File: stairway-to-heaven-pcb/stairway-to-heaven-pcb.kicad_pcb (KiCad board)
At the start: 2 copper layers, 99.8 x 97.3 mm, 67 parts, among them J1 Conn_01x04_Male, J10 Conn_01x04_Male, J11 Conn_01x04_Male, J12 Conn_01x04_Male, J13 Conn_01x04_Male, J14 Conn_01x04_Male, J15 PJ-063AH, J2 Conn_01x04_Male, J3 Conn_01x04_Male, J4 Conn_01x04_Male, J5 Conn_01x04_Male, J6 Conn_01x04_Male, J7 Conn_01x04_Male, J8 Conn_01x04_Male, J9 Conn_01x04_Male, Q1 FDN337N, Q10 FDN337N, Q11 FDN337N, Q12 FDN337N, Q13 FDN337N, Q14 FDN337N, Q15 FDN337N, Q16 FDN337N, Q17 FDN337N, Q18 FDN337N, Q19 FDN337N, Q2 FDN337N, Q20 FDN337N, Q21 FDN337N, Q22 FDN337N, Q23 FDN337N, Q24 FDN337N, Q25 FDN337N, Q26 FDN337N, Q27 FDN337N, Q28 FDN337N, Q29 FDN337N, Q3 FDN337N, Q30 FDN337N, Q31 FDN337N, Q32 FDN337N, Q33 FDN337N, Q34 FDN337N, Q35 FDN337N, Q36 FDN337N, Q37 FDN337N, Q38 FDN337N, Q39 FDN337N, Q4 FDN337N, Q40 FDN337N, Q41 FDN337N, Q42 FDN337N, Q5 FDN337N, Q6 FDN337N, Q7 FDN337N, Q8 FDN337N, Q9 FDN337N, U1 MEGA_PRO_EMBED_CH340G_{slash}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, U2 LM2575T-5.0

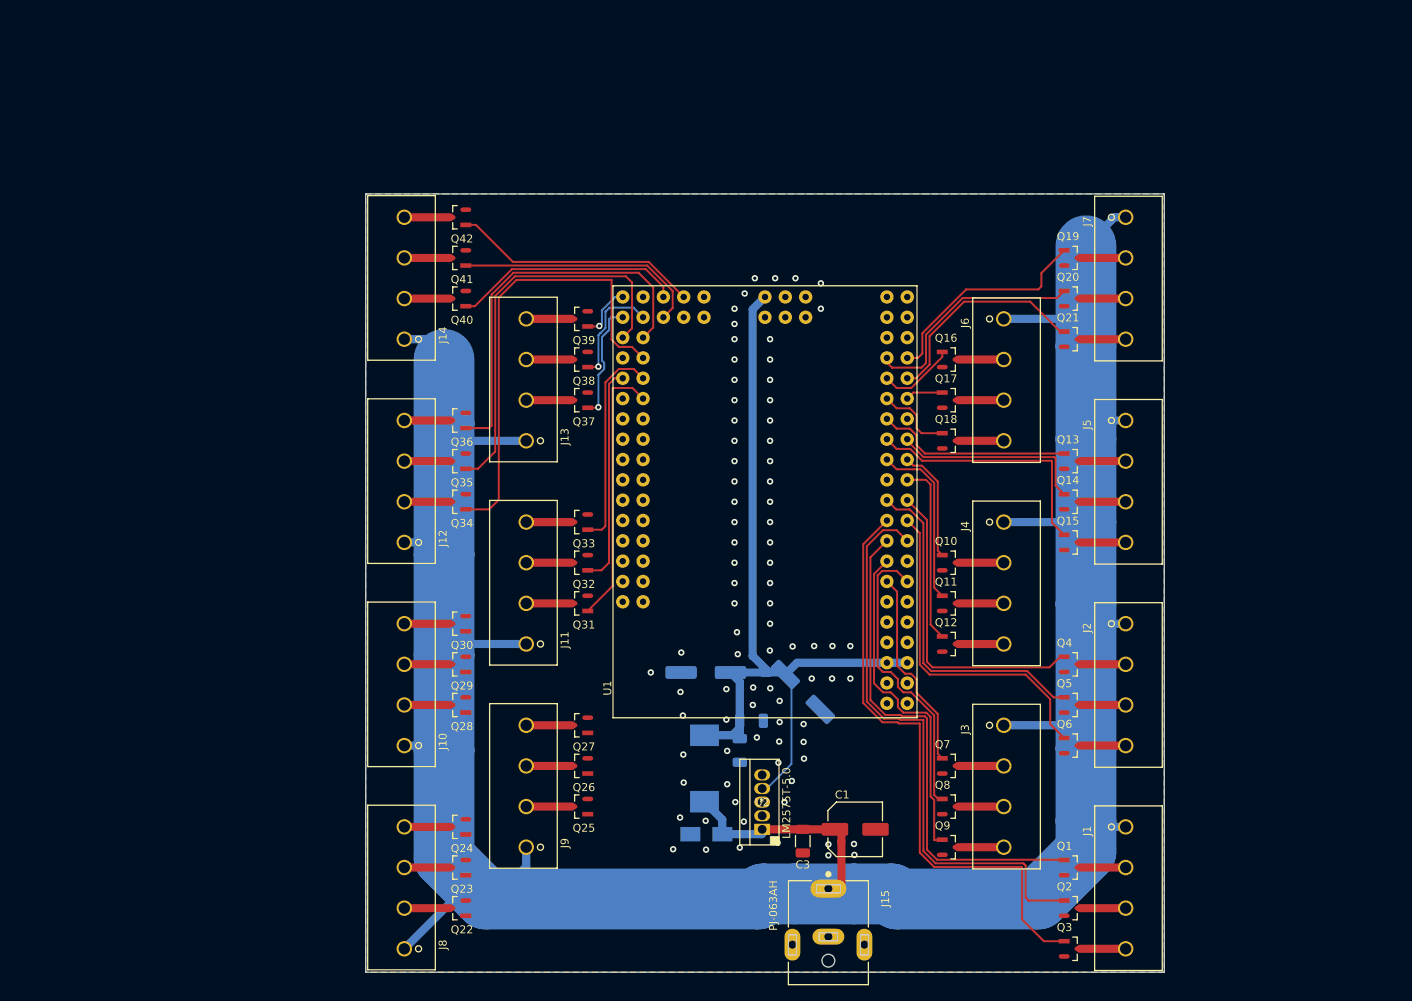
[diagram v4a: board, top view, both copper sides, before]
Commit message: replace 5V side, via galore, lots of ground areas checked, rest of the signals places
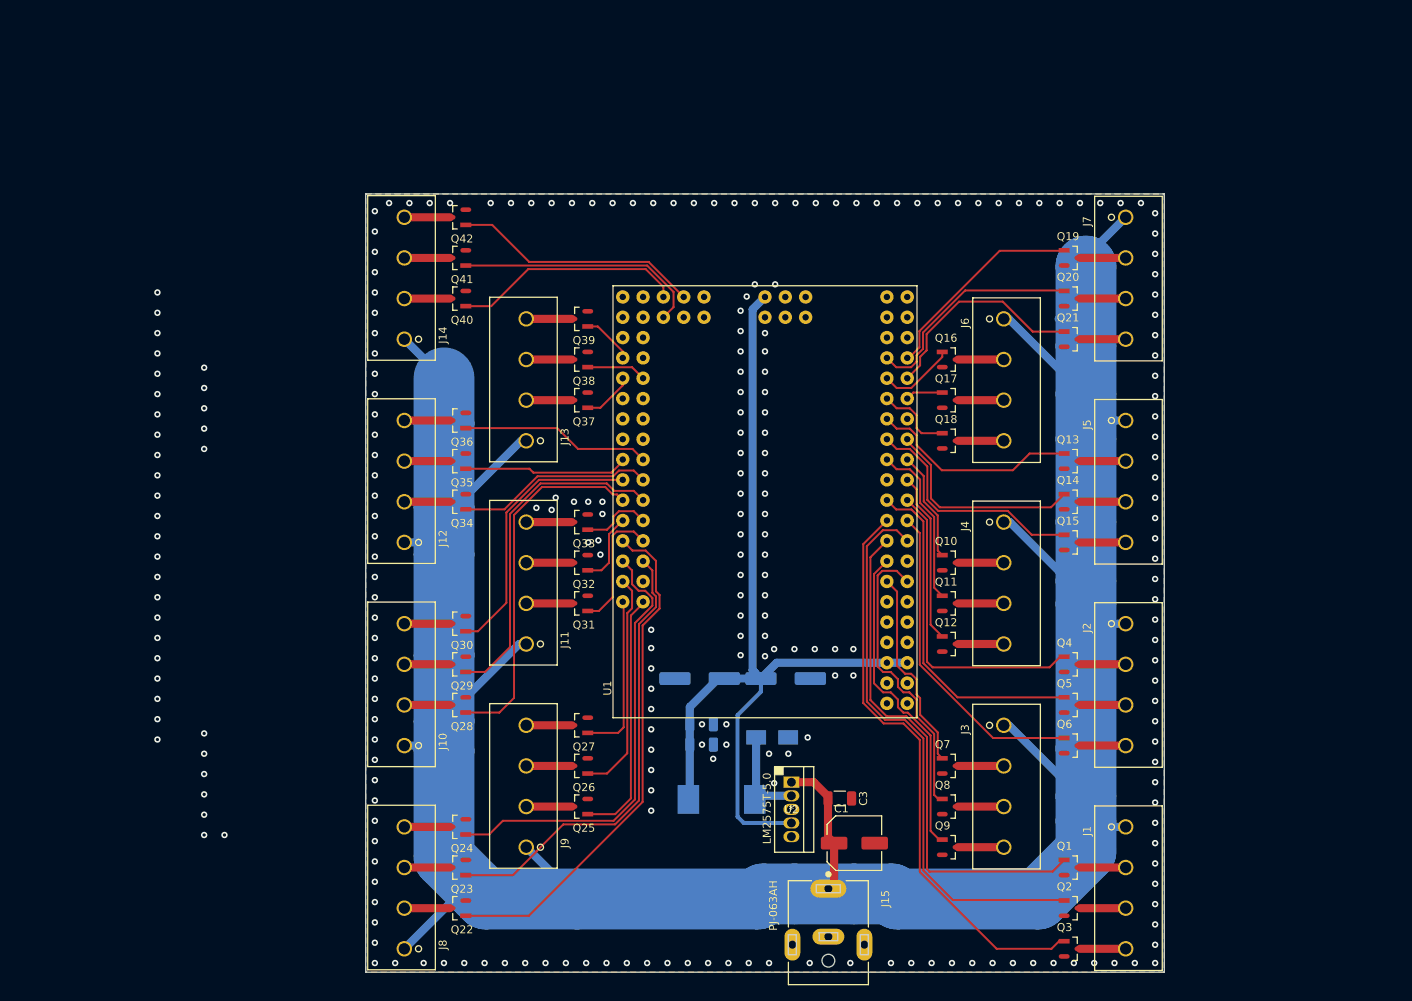
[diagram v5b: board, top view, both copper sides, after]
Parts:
- moved D1 14.6 mm to (152.0, 109.5), turned to 0 degrees
- moved C3 7.06 mm to (160.5, 117.1), turned to 180 degrees
- moved C6 6.26 mm to (143.2, 107.8)
- moved C5 4.83 mm to (143.2, 110.4), turned to 0 degrees
- moved L1 4.43 mm to (145.7, 117.2), turned to 180 degrees
- moved U2 3.77 mm to (154.4, 118.5), turned to 0 degrees
- moved C4 2.72 mm to (153.7, 102.1), turned to 0 degrees
- moved C1 1.73 mm to (162.3, 122.7)
- moved C2 1.08 mm to (143.0, 102.1)
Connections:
- Q25 pad 1: /Fets9/G_EN -> /LED9G_EN
- Q26 pad 1: /LED9R_EN -> /Fets9/R_EN
- U1 pad A0: unconnected-(U1-PadA0) -> /Fets9/B_EN
- U1 pad A1: unconnected-(U1-PadA1) -> /LED9G_EN
- U1 pad A10: unconnected-(U1-PadA10) -> /Fets10/G_EN
- U1 pad A11: unconnected-(U1-PadA11) -> /LED10R_EN
- U1 pad A12: unconnected-(U1-PadA12) -> /Fets10/B_EN
- U1 pad A13: unconnected-(U1-PadA13) -> /Fets12/G_EN
- U1 pad A14: unconnected-(U1-PadA14) -> /LED12R_EN
- U1 pad A15: unconnected-(U1-PadA15) -> /Fets12/B_EN
- U1 pad A2: unconnected-(U1-PadA2) -> /Fets9/R_EN
- U1 pad A4: unconnected-(U1-PadA4) -> /Fets8/B_EN
- U1 pad A5: unconnected-(U1-PadA5) -> /LED8R_EN
- U1 pad A6: unconnected-(U1-PadA6) -> /Fets8/G_EN
- U1 pad A7: unconnected-(U1-PadA7) -> /Fets11/G_EN
- U1 pad A8: unconnected-(U1-PadA8) -> /LED11R_EN
- U1 pad A9: unconnected-(U1-PadA9) -> /Fets11/B_EN
- U1 pad D27: /Fets8/B_EN -> unconnected-(U1-PadD27)
- U1 pad D28: /LED8R_EN -> unconnected-(U1-PadD28)
- U1 pad D29: /Fets8/G_EN -> unconnected-(U1-PadD29)
- U1 pad D30: /Fets9/B_EN -> unconnected-(U1-PadD30)
- U1 pad D31: /LED9R_EN -> unconnected-(U1-PadD31)
- U1 pad D32: /Fets9/G_EN -> unconnected-(U1-PadD32)
- U1 pad D34: /Fets10/B_EN -> unconnected-(U1-PadD34)
- U1 pad D35: /LED10R_EN -> unconnected-(U1-PadD35)
- U1 pad D36: /Fets10/G_EN -> unconnected-(U1-PadD36)
- U1 pad D37: /Fets11/G_EN -> unconnected-(U1-PadD37)
- U1 pad D38: /LED11R_EN -> /Fets13/G_EN
- U1 pad D39: /Fets11/B_EN -> /LED13R_EN
- U1 pad D40: unconnected-(U1-PadD40) -> /Fets13/B_EN
- U1 pad D41: /Fets12/G_EN -> unconnected-(U1-PadD41)
- U1 pad D42: /LED12R_EN -> unconnected-(U1-PadD42)
- U1 pad D43: /Fets12/B_EN -> unconnected-(U1-PadD43)
- U1 pad D44: /Fets13/G_EN -> unconnected-(U1-PadD44)
- U1 pad D45: /LED13R_EN -> unconnected-(U1-PadD45)
- U1 pad D46: /Fets13/B_EN -> unconnected-(U1-PadD46)
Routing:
- net /Fets8/G_EN: track 0.00 -> 64.4 mm
- net /LED8R_EN: track 0.00 -> 57.0 mm
- net /Fets8/B_EN: track 0.00 -> 55.7 mm
- net /Fets10/G_EN: track 0.00 -> 45.4 mm
- net /LED10R_EN: track 0.00 -> 42.5 mm
- net /Fets10/B_EN: track 0.00 -> 34.1 mm
- net /Fets12/G_EN: track 57.3 -> 24.7 mm
- net /LED9G_EN: track 0.00 -> 31.4 mm
- net /LED12R_EN: track 49.8 -> 20.6 mm
- net /Fets9/R_EN: track 0.00 -> 28.8 mm
- net +12V: track 356.4 -> 383.8 mm
- net /Fets12/B_EN: track 48.6 -> 23.8 mm
- net /Fets9/B_EN: track 0.00 -> 20.5 mm
- net /LED11R_EN: track 27.4 -> 9.05 mm
- net /Fets11/G_EN: track 33.5 -> 16.0 mm
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
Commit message: Vias galore
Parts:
- added R1: 0R, Resistor_SMD:R_1206_3216Metric, F.Cu at (169.5, 130.2)
- added R2: 0R, Resistor_SMD:R_1206_3216Metric, F.Cu at (130.3, 129.5)
- added R3: 0R, Resistor_SMD:R_1206_3216Metric, F.Cu at (169.5, 126.4)
- moved C1 0.89 mm to (162.3, 121.8)
- moved C3 0.63 mm to (160.5, 116.5)
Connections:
- U1 pad D23: /Fets7/B_EN -> unconnected-(U1-PadD23)
- U1 pad D24: /LED7R_EN -> unconnected-(U1-PadD24)
- U1 pad D25: /Fets7/G_EN -> unconnected-(U1-PadD25)
- U1 pad D29: unconnected-(U1-PadD29) -> /Fets7/B_EN
- U1 pad D30: unconnected-(U1-PadD30) -> /LED7R_EN
- U1 pad D31: unconnected-(U1-PadD31) -> /Fets7/G_EN
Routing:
- net /Fets7/B_EN: track 27.0 -> 20.4 mm
- net /LED1R_EN: track 70.5 -> 76.3 mm
- net /Fets1/B_EN: track 72.0 -> 77.0 mm
- net +12V: track 383.8 -> 378.9 mm
- net /LED7R_EN: track 28.3 -> 23.6 mm
- net /Fets7/G_EN: track 26.4 -> 22.0 mm
- net /Fets8/G_EN: track 64.4 -> 68.2 mm
- net /LED8R_EN: track 57.0 -> 60.8 mm
- net /Fets1/G_EN: track 64.1 -> 67.9 mm
- net /Fets5/B_EN: track 29.6 -> 32.1 mm
- net /Fets6/G_EN: track 9.66 -> 8.28 mm
- net /Fets3/G_EN: track 39.2 -> 40.0 mm
- net /Fets2/G_EN: track 25.4 -> 26.0 mm
- net GND: vias 256 -> 691

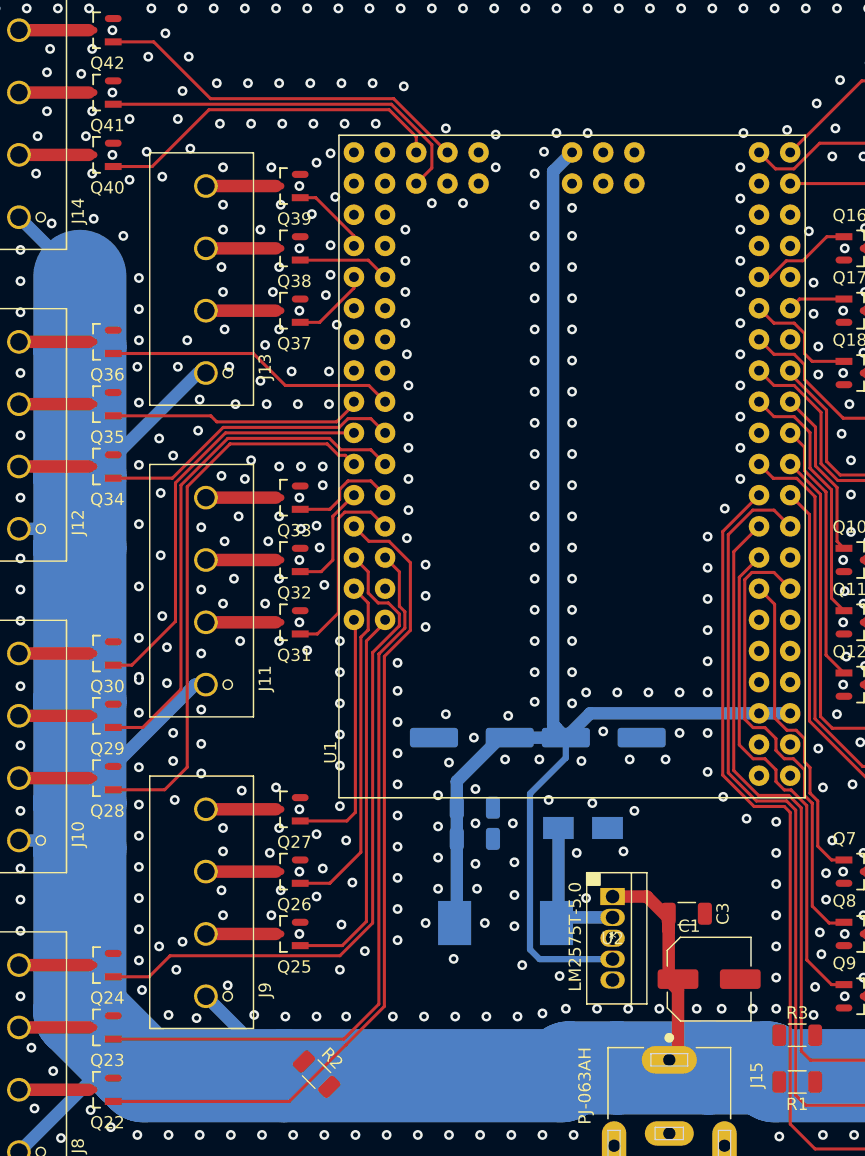
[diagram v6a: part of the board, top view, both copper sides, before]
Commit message: Pull-up resistors. Some sw work.
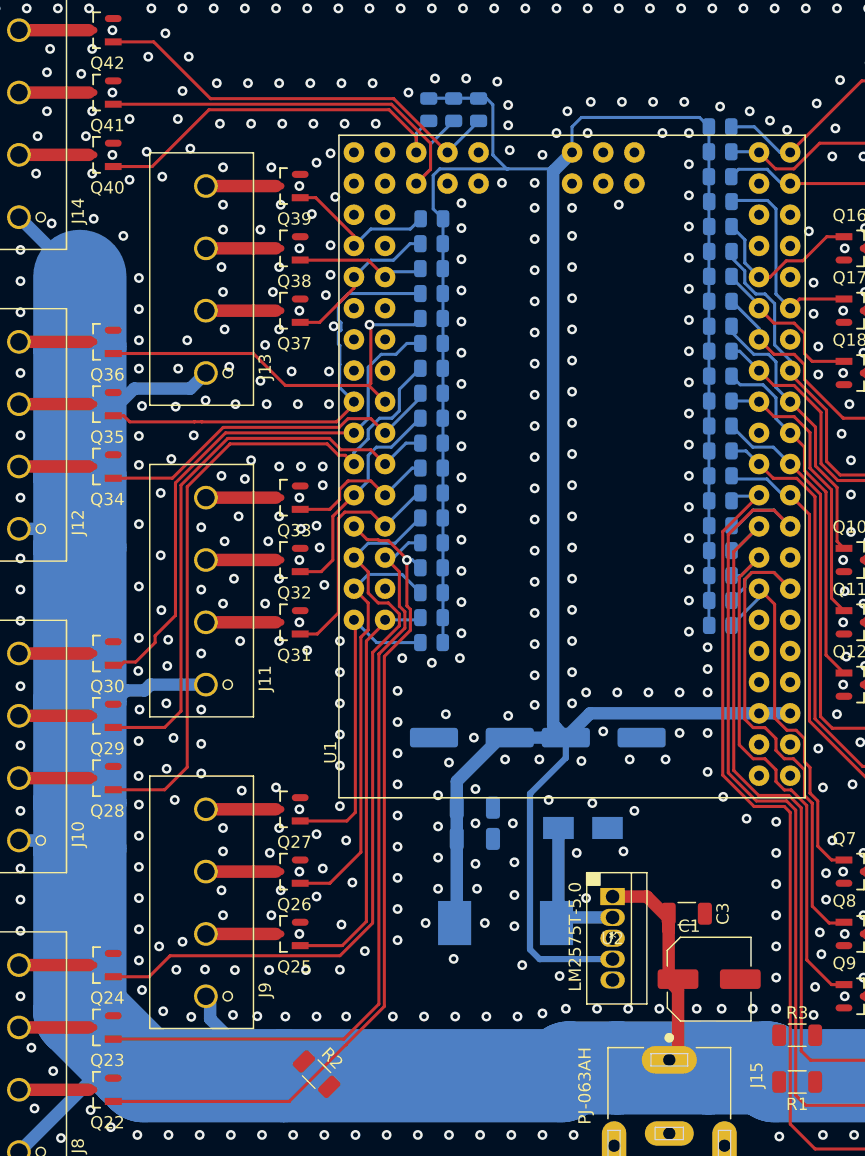
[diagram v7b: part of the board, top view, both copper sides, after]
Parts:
- added R10: 50k, Resistor_SMD:R_0805_2012Metric, B.Cu at (163.2, 93.0)
- added R11: 50k, Resistor_SMD:R_0805_2012Metric, B.Cu at (163.2, 90.9)
- added R12: 50k, Resistor_SMD:R_0805_2012Metric, B.Cu at (163.2, 88.9)
- added R13: 50k, Resistor_SMD:R_0805_2012Metric, B.Cu at (163.2, 68.6)
- added R14: 50k, Resistor_SMD:R_0805_2012Metric, B.Cu at (163.2, 74.7)
- added R15: 50k, Resistor_SMD:R_0805_2012Metric, B.Cu at (163.2, 72.6)
- added R16: 50k, Resistor_SMD:R_0805_2012Metric, B.Cu at (163.2, 66.5)
- added R17: 50k, Resistor_SMD:R_0805_2012Metric, B.Cu at (163.2, 62.5)
- added R18: 50k, Resistor_SMD:R_0805_2012Metric, B.Cu at (163.2, 70.6)
- added R19: 50k, Resistor_SMD:R_0805_2012Metric, B.Cu at (163.2, 60.5)
- added R20: 50k, Resistor_SMD:R_0805_2012Metric, B.Cu at (163.2, 58.4)
- added R21: 50k, Resistor_SMD:R_0805_2012Metric, B.Cu at (163.2, 64.5)
- added R22: 50k, Resistor_SMD:R_0805_2012Metric, B.Cu at (163.2, 52.3)
- added R23: 50k, Resistor_SMD:R_0805_2012Metric, B.Cu at (163.2, 54.4)
- added R24: 50k, Resistor_SMD:R_0805_2012Metric, B.Cu at (163.2, 56.4)
- added R25: 50k, Resistor_SMD:R_0805_2012Metric, B.Cu at (139.7, 88.3)
- added R26: 50k, Resistor_SMD:R_0805_2012Metric, B.Cu at (139.7, 86.2)
- added R27: 50k, Resistor_SMD:R_0805_2012Metric, B.Cu at (139.7, 84.2)
- added R28: 50k, Resistor_SMD:R_0805_2012Metric, B.Cu at (139.7, 92.3)
- added R29: 50k, Resistor_SMD:R_0805_2012Metric, B.Cu at (139.7, 90.3)
- added R30: 50k, Resistor_SMD:R_0805_2012Metric, B.Cu at (139.7, 94.4)
- added R31: 50k, Resistor_SMD:R_0805_2012Metric, B.Cu at (139.7, 72.0)
- added R32: 50k, Resistor_SMD:R_0805_2012Metric, B.Cu at (139.7, 78.1)
- added R33: 50k, Resistor_SMD:R_0805_2012Metric, B.Cu at (139.7, 70.0)
- added R34: 50k, Resistor_SMD:R_0805_2012Metric, B.Cu at (139.7, 82.2)
- added R35: 50k, Resistor_SMD:R_0805_2012Metric, B.Cu at (139.7, 76.1)
- added R36: 50k, Resistor_SMD:R_0805_2012Metric, B.Cu at (139.7, 80.1)
- added R37: 50k, Resistor_SMD:R_0805_2012Metric, B.Cu at (139.7, 74.0)
- added R38: 50k, Resistor_SMD:R_0805_2012Metric, B.Cu at (139.7, 65.9)
- added R39: 50k, Resistor_SMD:R_0805_2012Metric, B.Cu at (139.7, 67.9)
- added R4: 50k, Resistor_SMD:R_0805_2012Metric, B.Cu at (163.2, 86.9)
- added R40: 50k, Resistor_SMD:R_0805_2012Metric, B.Cu at (139.7, 61.8)
- added R41: 50k, Resistor_SMD:R_0805_2012Metric, B.Cu at (139.7, 63.9)
- added R42: 50k, Resistor_SMD:R_0805_2012Metric, B.Cu at (139.7, 59.8)
- added R43: 50k, Resistor_SMD:R_0805_2012Metric, B.Cu at (139.4, 50.9)
- added R44: 50k, Resistor_SMD:R_0805_2012Metric, B.Cu at (141.5, 50.9)
- added R45: 50k, Resistor_SMD:R_0805_2012Metric, B.Cu at (143.5, 50.9)
- added R5: 50k, Resistor_SMD:R_0805_2012Metric, B.Cu at (163.2, 84.8)
- added R6: 50k, Resistor_SMD:R_0805_2012Metric, B.Cu at (163.2, 82.8)
- added R7: 50k, Resistor_SMD:R_0805_2012Metric, B.Cu at (163.2, 76.7)
- added R8: 50k, Resistor_SMD:R_0805_2012Metric, B.Cu at (163.2, 78.7)
- added R9: 50k, Resistor_SMD:R_0805_2012Metric, B.Cu at (163.2, 80.8)
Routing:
- net +5V: track 114.3 -> 227.9 mm
- net /LED12R_EN: track 20.6 -> 36.4 mm
- net /LED6R_EN: track 4.69 -> 17.2 mm
- net /LED5R_EN: track 26.4 -> 38.6 mm
- net /Fets10/B_EN: track 34.1 -> 45.0 mm
- net /Fets10/G_EN: track 45.4 -> 56.0 mm
- net /Fets12/B_EN: track 23.8 -> 33.2 mm, vias 0 -> 1
- net /LED11R_EN: track 9.05 -> 18.3 mm
- net /Fets4/G_EN: track 13.8 -> 22.6 mm
- net /Fets4/B_EN: track 21.4 -> 29.1 mm
- net /Fets8/B_EN: track 55.7 -> 62.4 mm
- net /LED2R_EN: track 37.6 -> 44.2 mm
- net /Fets13/G_EN: track 6.43 -> 13.0 mm
- net /Fets9/R_EN: track 28.8 -> 35.3 mm
- net /Fets13/B_EN: track 6.49 -> 12.8 mm
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
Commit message: vias
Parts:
- added R46: 0R, Resistor_SMD:R_1206_3216Metric, B.Cu at (160.7, 104.6)
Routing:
- net +5V: track 227.9 -> 195.5 mm
- net GND: vias 713 -> 683
